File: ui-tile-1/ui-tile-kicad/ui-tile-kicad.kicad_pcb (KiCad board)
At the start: 4 copper layers, 72.4 x 87.3 mm, 64 parts, among them Q1 2N7002, SW1 SKRPABE010, SW2 SKRPABE010, SW3 EC11E15244G1, SW4 EC11E15244G1, SW5 EC11E15244G1, SW6 EC11E15244G1, U1 RP2040, U2 W25Q16JVUXIQ, U3 NCP1117ST33T3G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

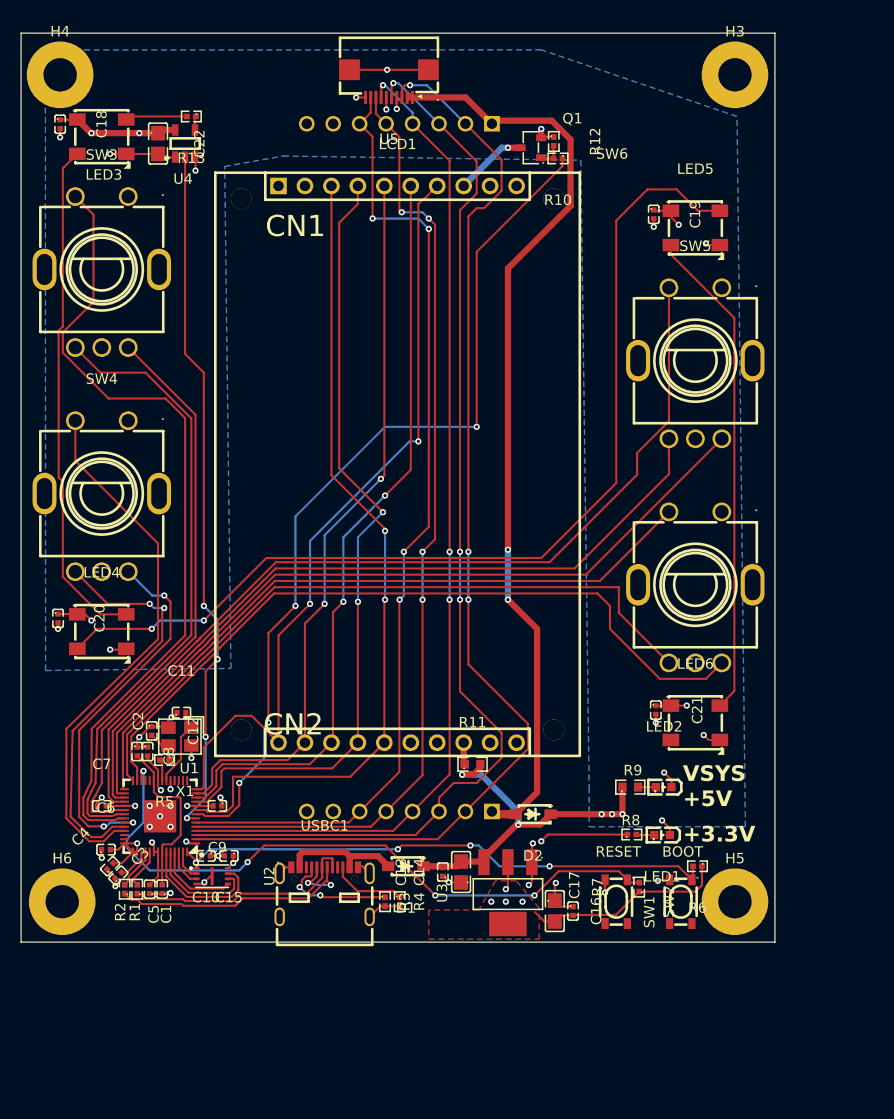
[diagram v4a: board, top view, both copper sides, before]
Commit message: added some labeling
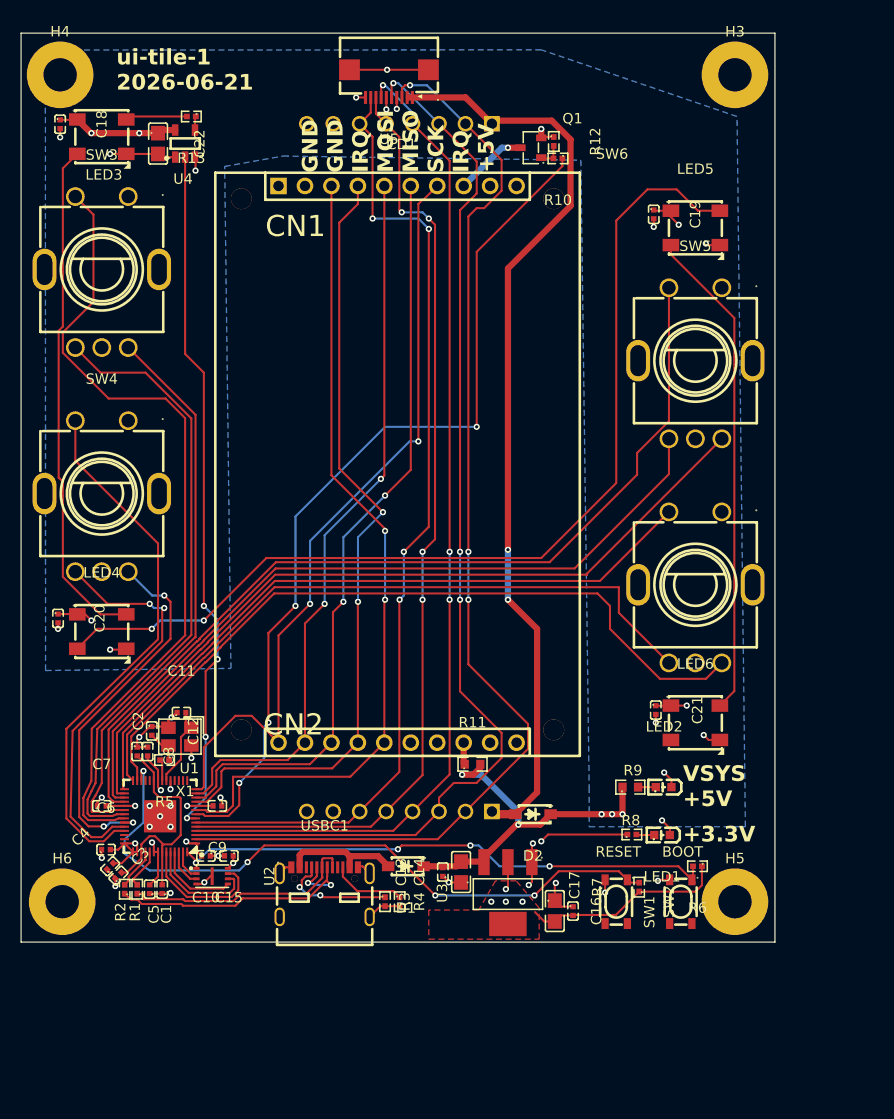
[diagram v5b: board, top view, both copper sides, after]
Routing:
- net +1V1: track 19.6 -> 23.0 mm
- net /rp2040/RUN: track 63.5 -> 64.0 mm
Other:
- board text added: "GND GND IRQ MOSI MISO SCK IRQ +5V"
- board text added: "ui-tile-1 2026-06-21"
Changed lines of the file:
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@@
 		)
 		(property "Value" "470"
-			(at 0 4 0)
+			(at -2.8 0 0)
 			(layer "F.Fab")
 			(effects
@@
 		)
 	)
+	(gr_text "ui-tile-1\n2026-06-21"
+		(at 104.4 60.4 0)
+		(layer "F.SilkS")
+		(effects
+			(font
+				(size 1.5 1.5)
+				(thickness 0.3)
+				(bold yes)
+			)
+			(justify left bottom)
+		)
+	)
 	(gr_text "VSYS\n+5V\n"
 		(at 158.8 129.2 0)
@@
 		)
 	)
+	(gr_text "GND\nGND\nIRQ\nMOSI\nMISO\nSCK\nIRQ\n+5V\n"
+		(at 140.8 68.2 90)
+		(layer "F.SilkS")
+		(effects
+			(font
+				(size 1.5 1.5)
+				(thickness 0.3)
+				(bold yes)
+			)
+			(justify left bottom)
+		)
+	)
 	(segment
 		(start 108.8 137.42)
@@
 	)
 	(segment
-		(start 106.4 132.599235)
-		(end 106.397586 132.596821)
+		(start 111.2 132.4)
+		(end 111.177289 132.422711)
 		(width 0.2)
 		(layer "F.Cu")
@@
 	)
 	(segment
-		(start 111.2 132.4)
-		(end 111.177289 132.422711)
+		(start 106.4 132.599235)
+		(end 106.4 133.42)
 		(width 0.2)
 		(layer "F.Cu")
@@
 	)
 	(segment
-		(start 106.4 133.42)
-		(end 106.4 132.599235)
-		(width 0.2)
-		(layer "F.Cu")
-		(net "+3V3")
-	)
-	(segment
 		(start 105.18 129)
 		(end 106.2 129)
@@
 	)
 	(segment
-		(start 106.394407 132.6)
-		(end 106.397586 132.596821)
-		(width 0.2)
-		(layer "F.Cu")
-		(net "+3V3")
-	)
-	(segment
 		(start 104.096985 134.503015)
 		(end 104.916985 134.503015)
@@
 	)
 	(segment
-		(start 105.18 132.6)
-		(end 106.394407 132.6)
-		(width 0.2)
-		(layer "F.Cu")
-		(net "+3V3")
-	)
-	(segment
 		(start 148.25 139.52)
 		(end 148.295 139.475)
@@
 	)
 	(segment
+		(start 106.394407 132.6)
+		(end 105.18 132.6)
+		(width 0.2)
+		(layer "F.Cu")
+		(net "+3V3")
+	)
+	(segment
 		(start 111.194493 129.000674)
 		(end 111.199326 129.000674)
@@
 	)
 	(segment
+		(start 106.2 132.6)
+		(end 106.4 132.599235)
+		(width 0.2)
+		(layer "F.Cu")
+		(net "+3V3")
+	)
+	(segment
 		(start 111.199326 129.000674)
 		(end 111.2 129)
@@
 		(net "+3V3")
 	)
+	(segment
+		(start 106.2 132.6)
+		(end 106.394407 132.6)
+		(width 0.2)
+		(layer "F.Cu")
+		(net "+3V3")
+	)
 	(via
 		(at 140.4 138.2)
@@
 	)
 	(via
-		(at 106.397586 132.596821)
+		(at 106.2 132.6)
 		(size 0.6)
 		(drill 0.3)
@@
 	)
 	(segment
+		(start 106.8 133.42)
+		(end 106.8 132.684472)
+		(width 0.2)
+		(layer "F.Cu")
+		(net "+1V1")
+	)
+	(segment
+		(start 108.11529 131.91029)
+		(end 108.9 132.695)
+		(width 0.2)
+		(layer "F.Cu")
+		(net "+1V1")
+	)
+	(segment
 		(start 108.8 132.795)
 		(end 108.9 132.695)
@@
 	)
 	(segment
+		(start 106.8 132.684472)
+		(end 107.574182 131.91029)
+		(width 0.2)
+		(layer "F.Cu")
+		(net "+1V1")
+	)
+	(segment
 		(start 108 125.8)
 		(end 106.4 124.2)
@@
 	)
 	(segment
+		(start 107.574182 131.91029)
+		(end 108.11529 131.91029)
+		(width 0.2)
+		(layer "F.Cu")
+		(net "+1V1")
+	)
+	(segment
 		(start 109.705 132.695)
 		(end 110.6 131.8)
@@
 	)
 	(segment
-		(start 116.2 135.2)
-		(end 117 134.4)
-		(width 0.2)
-		(layer "B.Cu")
-		(net "/rp2040/RUN")
-	)
-	(segment
-		(start 107 130.6)
-		(end 105.4 132.2)
+		(start 105.2 132.2)
+		(end 105.2 133.6)
 		(width 0.2)
 		(layer "B.Cu")
@@
 	)
 	(segment
-		(start 105.4 133)
+		(start 105.2 133.6)
 		(end 107.6 135.2)
 		(width 0.2)
@@
 	)
 	(segment
-		(start 135.025 137.6)
-		(end 144.551471 137.6)
+		(start 107 130.6)
+		(end 105.2 132.2)
+		(width 0.2)
+		(layer "B.Cu")
+		(net "/rp2040/RUN")
+	)
+	(segment
+		(start 116.2 135.2)
+		(end 117 134.4)
 		(width 0.2)
 		(layer "B.Cu")
@@
 	)
 	(segment
-		(start 105.4 132.2)
-		(end 105.4 133)
+		(start 135.025 137.6)
+		(end 144.551471 137.6)
 		(width 0.2)
 		(layer "B.Cu")
@@
 	)
 	(segment
+		(start 127.762 63.5)
+		(end 128.825 62.437)
+		(width 0.2)
+		(layer "F.Cu")
+		(net "/headers/IRQ")
+	)
+	(segment
 		(start 131.57 125.732)
 		(end 131.57 109.23)
@@
 	)
 	(segment
-		(start 128.825 62.437)
-		(end 128.825 60.975)
-		(width 0.2)
-		(layer "F.Cu")
-		(net "/headers/IRQ")
-	)
-	(segment
 		(start 126.702 130.6)
 		(end 127.762 129.54)
@@
 	)
 	(segment
-		(start 127.762 63.5)
-		(end 128.825 62.437)
-		(width 0.2)
-		(layer "F.Cu")
-		(net "/headers/IRQ")
-	)
-	(segment
 		(start 132 104.6)
 		(end 134.4 102.2)
@@
 		(net "/headers/IRQ")
 	)
+	(segment
+		(start 128.825 62.437)
+		(end 128.825 60.975)
+		(width 0.2)
+		(layer "F.Cu")
+		(net "/headers/IRQ")
+	)
 	(via
 		(at 131.6 109.2)
@@
 		)
 		(min_thickness 0.25)
-		(fill
+		(fill yes
 			(thermal_gap 0.5)
 			(thermal_bridge_width 0.5)
